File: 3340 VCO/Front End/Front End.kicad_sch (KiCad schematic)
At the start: 32 parts, among them J1 AudioJack2_SwitchT, J2 AudioJack2_SwitchT, J3 AudioJack2_SwitchT, J4 AudioJack2_SwitchT, J5 AudioJack2_SwitchT, J6 Conn_01x19, J7 AudioJack2_SwitchT, J8 AudioJack2_SwitchT, J9 AudioJack2_SwitchT, SW1 SW_SPDT

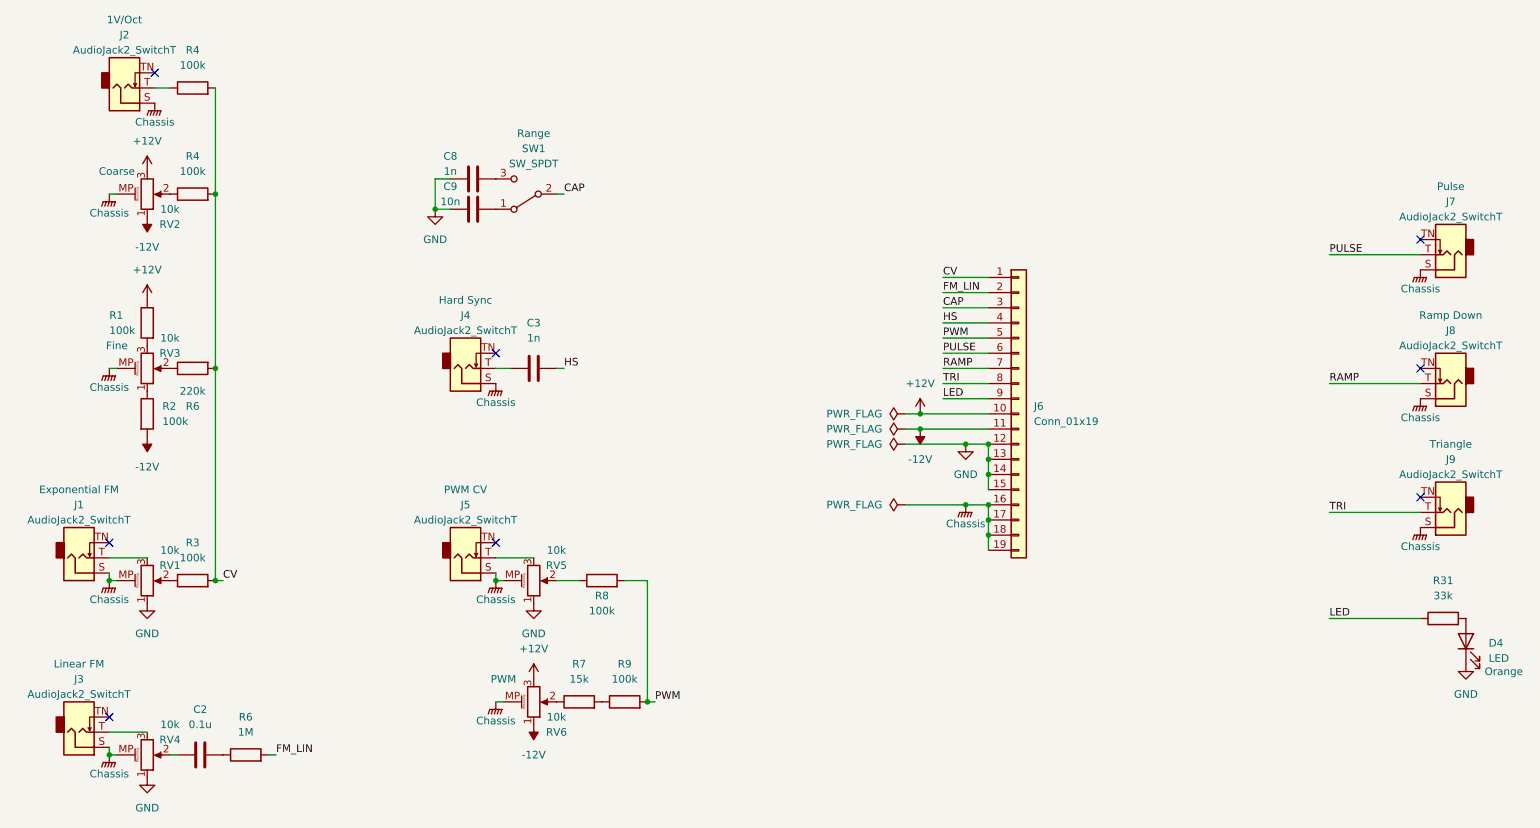
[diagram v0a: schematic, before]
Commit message: Add precision R and C notes, update -5V regulator
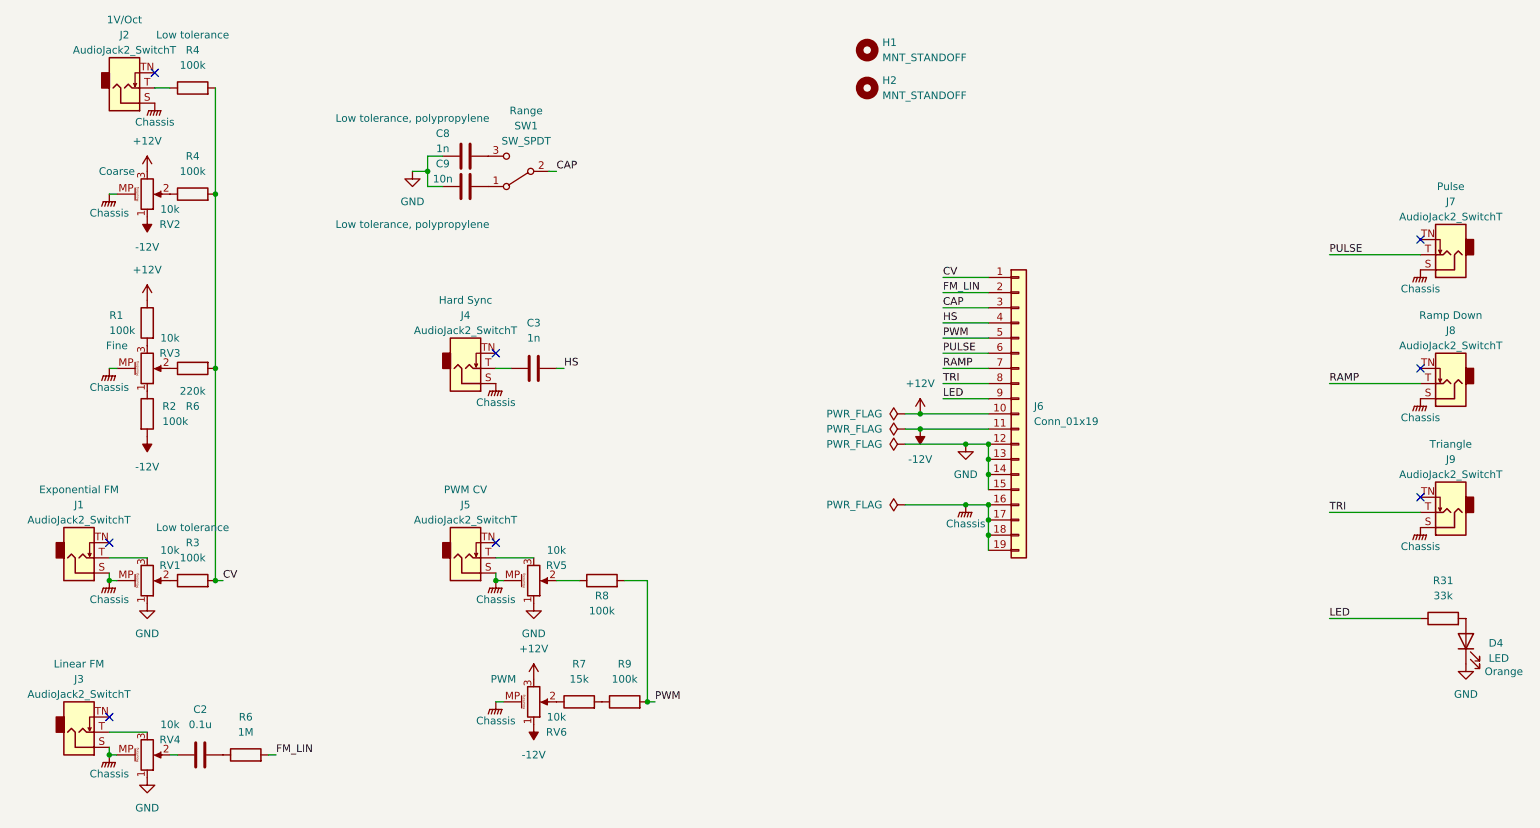
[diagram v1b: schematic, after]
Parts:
- added H1, H2: MNT_STANDOFF, 0_MountingHole:MountingHole_Pitch7.5mm_Drill3.4mm, symbol Mechanical:MountingHole
- C8, C9: Notes (none) -> Low tolerance, polypropylene
- R3, R4: Notes (none) -> Low tolerance
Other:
- moved on the sheet: C8, C9, SW1
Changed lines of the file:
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@@
   (junction (at 34.29 124.46) (diameter 0) (color 0 0 0 0)
   )
+  (junction (at 87.63 55.88) (diameter 0) (color 0 0 0 0)
+  )
   (junction (at 124.46 144.78) (diameter 0) (color 0 0 0 0)
   )
@@
   )
   (junction (at 177.8 101.6) (diameter 0) (color 0 0 0 0)
-  )
-  (junction (at 88.9 62.23) (diameter 0) (color 0 0 0 0)
   )
   (junction (at 181.61 114.3) (diameter 0) (color 0 0 0 0)
@@
     (stroke (width 0) (type default))
   )
-  (wire (pts (xy 88.9 57.15) (xy 88.9 62.23))
+  (wire (pts (xy 87.63 53.34) (xy 87.63 55.88))
     (stroke (width 0) (type default))
   )
@@
     (stroke (width 0) (type default))
   )
+  (wire (pts (xy 87.63 55.88) (xy 87.63 58.42))
+    (stroke (width 0) (type default))
+  )
   (wire (pts (xy 181.61 104.14) (xy 181.61 106.68))
     (stroke (width 0) (type default))
@@
     (stroke (width 0) (type default))
   )
+  (wire (pts (xy 85.09 55.88) (xy 87.63 55.88))
+    (stroke (width 0) (type default))
+  )
   (wire (pts (xy 124.46 144.78) (xy 125.73 144.78))
     (stroke (width 0) (type default))
@@
     (stroke (width 0) (type default))
   )
-  (wire (pts (xy 88.9 57.15) (xy 91.44 57.15))
-    (stroke (width 0) (type default))
-  )
-  (wire (pts (xy 110.49 59.69) (xy 109.22 59.69))
+  (wire (pts (xy 87.63 53.34) (xy 90.17 53.34))
+    (stroke (width 0) (type default))
+  )
+  (wire (pts (xy 109.22 55.88) (xy 107.95 55.88))
     (stroke (width 0) (type default))
   )
@@
     (stroke (width 0) (type default))
   )
-  (wire (pts (xy 88.9 62.23) (xy 91.44 62.23))
+  (wire (pts (xy 87.63 58.42) (xy 90.17 58.42))
     (stroke (width 0) (type default))
   )
@@
     (effects (font (size 1.27 1.27)) (justify left bottom))
   )
-  (label "CAP" (at 110.49 59.69 0) (fields_autoplaced)
+  (label "CAP" (at 109.22 55.88 0) (fields_autoplaced)
     (effects (font (size 1.27 1.27)) (justify left bottom))
   )
@@
     (effects (font (size 1.27 1.27)) (justify left bottom))
   )
-  (symbol (lib_id "Switch:SW_SPDT") (at 104.14 59.69 180) (unit 1)
-    (in_bom yes) (on_board yes) (dnp no)
-    (property "Reference" "SW1" (at 105.41 52.07 0)
-      (effects (font (size 1.27 1.27)))
-    )
-    (property "Value" "SW_SPDT" (at 105.41 54.61 0)
-      (effects (font (size 1.27 1.27)))
-    )
-    (property "Footprint" "0_Switch_THT:MTS-102_MTS-103_MTS-112_MTS-113_MTS-123" (at 104.14 59.69 0)
-      (effects (font (size 1.27 1.27)) hide)
-    )
-    (property "Datasheet" "~" (at 104.14 59.69 0)
-      (effects (font (size 1.27 1.27)) hide)
-    )
-    (property "Notes" "Range" (at 105.41 49.53 0)
+  (symbol (lib_id "Switch:SW_SPDT") (at 102.87 55.88 180) (unit 1)
+    (in_bom yes) (on_board yes) (dnp no)
+    (property "Reference" "SW1" (at 104.14 48.26 0)
+      (effects (font (size 1.27 1.27)))
+    )
+    (property "Value" "SW_SPDT" (at 104.14 50.8 0)
+      (effects (font (size 1.27 1.27)))
+    )
+    (property "Footprint" "0_Switch_THT:MTS-102_MTS-103_MTS-112_MTS-113_MTS-123" (at 102.87 55.88 0)
+      (effects (font (size 1.27 1.27)) hide)
+    )
+    (property "Datasheet" "~" (at 102.87 55.88 0)
+      (effects (font (size 1.27 1.27)) hide)
+    )
+    (property "Notes" "Range" (at 104.14 45.72 0)
       (effects (font (size 1.27 1.27)))
     )
@@
         (path "/a1c7a80e-571d-4d37-b0fe-6f3972cbd9bc"
           (reference "#PWR010") (unit 1)
+        )
+      )
+    )
+  )
+  (symbol (lib_id "Mechanical:MountingHole") (at 161.29 35.56 0) (unit 1)
+    (in_bom yes) (on_board yes) (dnp no) (fields_autoplaced)
+    (property "Reference" "H1" (at 163.83 34.29 0)
+      (effects (font (size 1.27 1.27)) (justify left))
+    )
+    (property "Value" "MNT_STANDOFF" (at 163.83 36.83 0)
+      (effects (font (size 1.27 1.27)) (justify left))
+    )
+    (property "Footprint" "0_MountingHole:MountingHole_Pitch7.5mm_Drill3.4mm" (at 161.29 35.56 0)
+      (effects (font (size 1.27 1.27)) hide)
+    )
+    (property "Datasheet" "~" (at 161.29 35.56 0)
+      (effects (font (size 1.27 1.27)) hide)
+    )
+    (instances
+      (project "Front End"
+        (path "/a1c7a80e-571d-4d37-b0fe-6f3972cbd9bc"
+          (reference "H1") (unit 1)
         )
       )
@@
     )
   )
-  (symbol (lib_id "Device:C") (at 95.25 62.23 90) (unit 1)
-    (in_bom yes) (on_board yes) (dnp no)
-    (property "Reference" "C9" (at 91.44 58.42 90)
-      (effects (font (size 1.27 1.27)))
-    )
-    (property "Value" "10n" (at 91.44 60.96 90)
-      (effects (font (size 1.27 1.27)))
-    )
-    (property "Footprint" "0_Capacitor_THT:C_Disc_D5.5mm_W2.5mm_P2.50mm" (at 99.06 61.2648 0)
-      (effects (font (size 1.27 1.27)) hide)
-    )
-    (property "Datasheet" "~" (at 95.25 62.23 0)
-      (effects (font (size 1.27 1.27)) hide)
+  (symbol (lib_id "Device:C") (at 93.98 58.42 90) (unit 1)
+    (in_bom yes) (on_board yes) (dnp no)
+    (property "Reference" "C9" (at 90.17 54.61 90)
+      (effects (font (size 1.27 1.27)))
+    )
+    (property "Value" "10n" (at 90.17 57.15 90)
+      (effects (font (size 1.27 1.27)))
+    )
+    (property "Footprint" "0_Capacitor_THT:C_Disc_D5.5mm_W2.5mm_P2.50mm" (at 97.79 57.4548 0)
+      (effects (font (size 1.27 1.27)) hide)
+    )
+    (property "Datasheet" "~" (at 93.98 58.42 0)
+      (effects (font (size 1.27 1.27)) hide)
+    )
+    (property "Notes" "Low tolerance, polypropylene" (at 85.09 64.77 90)
+      (effects (font (size 1.27 1.27)))
     )
     (pin "1")
@@
         (path "/a1c7a80e-571d-4d37-b0fe-6f3972cbd9bc"
           (reference "#FLG04") (unit 1)
+        )
+      )
+    )
+  )
+  (symbol (lib_id "Mechanical:MountingHole") (at 161.29 41.91 0) (unit 1)
+    (in_bom yes) (on_board yes) (dnp no) (fields_autoplaced)
+    (property "Reference" "H2" (at 163.83 40.64 0)
+      (effects (font (size 1.27 1.27)) (justify left))
+    )
+    (property "Value" "MNT_STANDOFF" (at 163.83 43.18 0)
+      (effects (font (size 1.27 1.27)) (justify left))
+    )
+    (property "Footprint" "0_MountingHole:MountingHole_Pitch7.5mm_Drill3.4mm" (at 161.29 41.91 0)
+      (effects (font (size 1.27 1.27)) hide)
+    )
+    (property "Datasheet" "~" (at 161.29 41.91 0)
+      (effects (font (size 1.27 1.27)) hide)
+    )
+    (instances
+      (project "Front End"
+        (path "/a1c7a80e-571d-4d37-b0fe-6f3972cbd9bc"
+          (reference "H2") (unit 1)
         )
       )
@@
       (effects (font (size 1.27 1.27)) hide)
     )
+    (property "Notes" "Low tolerance" (at 48.26 33.02 90)
+      (effects (font (size 1.27 1.27)))
+    )
     (pin "1")
     (pin "2")
@@
     )
   )
-  (symbol (lib_id "Device:C") (at 95.25 57.15 90) (unit 1)
-    (in_bom yes) (on_board yes) (dnp no)
-    (property "Reference" "C8" (at 91.44 53.34 90)
-      (effects (font (size 1.27 1.27)))
-    )
-    (property "Value" "1n" (at 91.44 55.88 90)
-      (effects (font (size 1.27 1.27)))
-    )
-    (property "Footprint" "0_Capacitor_THT:C_Disc_D5.5mm_W2.5mm_P2.50mm" (at 99.06 56.1848 0)
-      (effects (font (size 1.27 1.27)) hide)
-    )
-    (property "Datasheet" "~" (at 95.25 57.15 0)
-      (effects (font (size 1.27 1.27)) hide)
+  (symbol (lib_id "Device:C") (at 93.98 53.34 90) (unit 1)
+    (in_bom yes) (on_board yes) (dnp no)
+    (property "Reference" "C8" (at 90.17 49.53 90)
+      (effects (font (size 1.27 1.27)))
+    )
+    (property "Value" "1n" (at 90.17 52.07 90)
+      (effects (font (size 1.27 1.27)))
+    )
+    (property "Footprint" "0_Capacitor_THT:C_Disc_D5.5mm_W2.5mm_P2.50mm" (at 97.79 52.3748 0)
+      (effects (font (size 1.27 1.27)) hide)
+    )
+    (property "Datasheet" "~" (at 93.98 53.34 0)
+      (effects (font (size 1.27 1.27)) hide)
+    )
+    (property "Notes" "Low tolerance, polypropylene" (at 85.09 46.99 90)
+      (effects (font (size 1.27 1.27)))
     )
     (pin "1")
@@
     )
   )
-  (symbol (lib_id "power:GND") (at 88.9 62.23 0) (unit 1)
-    (in_bom yes) (on_board yes) (dnp no) (fields_autoplaced)
-    (property "Reference" "#PWR020" (at 88.9 68.58 0)
-      (effects (font (size 1.27 1.27)) hide)
-    )
-    (property "Value" "GND" (at 88.9 67.31 0)
-      (effects (font (size 1.27 1.27)))
-    )
-    (property "Footprint" "" (at 88.9 62.23 0)
-      (effects (font (size 1.27 1.27)) hide)
-    )
-    (property "Datasheet" "" (at 88.9 62.23 0)
+  (symbol (lib_id "power:GND") (at 85.09 55.88 0) (unit 1)
+    (in_bom yes) (on_board yes) (dnp no) (fields_autoplaced)
+    (property "Reference" "#PWR020" (at 85.09 62.23 0)
+      (effects (font (size 1.27 1.27)) hide)
+    )
+    (property "Value" "GND" (at 85.09 60.96 0)
+      (effects (font (size 1.27 1.27)))
+    )
+    (property "Footprint" "" (at 85.09 55.88 0)
+      (effects (font (size 1.27 1.27)) hide)
+    )
+    (property "Datasheet" "" (at 85.09 55.88 0)
       (effects (font (size 1.27 1.27)) hide)
     )
@@
       (effects (font (size 1.27 1.27)) hide)
     )
-    (pin "1")
+    (property "Notes" "Low tolerance" (at 48.26 115.57 90)
+      (effects (font (size 1.27 1.27)))
+    )
+    (pin "1")

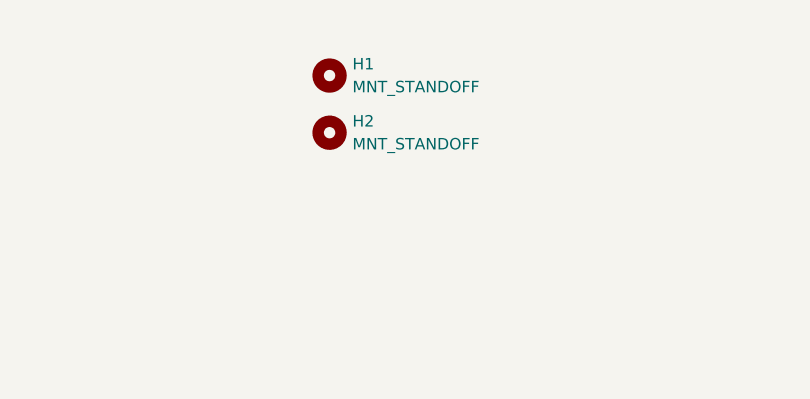
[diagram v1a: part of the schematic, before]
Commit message: Update VCO capacitor selection
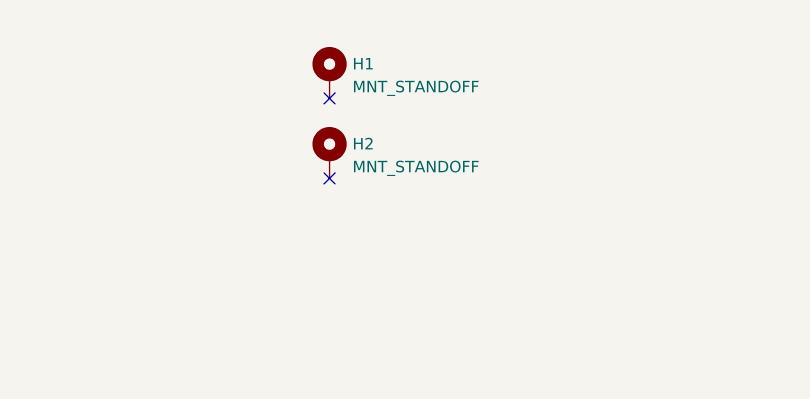
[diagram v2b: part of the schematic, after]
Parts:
- C8: footprint 0_Capacitor_THT:C_Disc_D5.5mm_W2.5mm_P2.50mm -> 0_Capacitor_THT:C_Rect_L7.2mm_W4.5mm_P5.00mm
- C9: footprint 0_Capacitor_THT:C_Disc_D5.5mm_W2.5mm_P2.50mm -> 0_Capacitor_THT:C_Rect_L7.5mm_W5.5mm_P5.00mm
- H1, H2: symbol Mechanical:MountingHole -> Mechanical:MountingHole_Pad
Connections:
- no-connect marks 8 -> 10
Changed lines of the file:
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@@
   (no_connect (at 41.91 39.37))
   (no_connect (at 99.06 118.11))
+  (no_connect (at 161.29 38.1))
+  (no_connect (at 161.29 46.99))
   (no_connect (at 34.29 147.32))
   (no_connect (at 34.29 118.11))
@@
     )
   )
-  (symbol (lib_id "Mechanical:MountingHole") (at 161.29 35.56 0) (unit 1)
+  (symbol (lib_id "Mechanical:MountingHole_Pad") (at 161.29 35.56 0) (unit 1)
     (in_bom yes) (on_board yes) (dnp no) (fields_autoplaced)
     (property "Reference" "H1" (at 163.83 34.29 0)
@@
       (effects (font (size 1.27 1.27)) hide)
     )
+    (pin "1")
     (instances
       (project "Front End"
@@
       (effects (font (size 1.27 1.27)))
     )
-    (property "Footprint" "0_Capacitor_THT:C_Disc_D5.5mm_W2.5mm_P2.50mm" (at 97.79 57.4548 0)
+    (property "Footprint" "0_Capacitor_THT:C_Rect_L7.5mm_W5.5mm_P5.00mm" (at 97.79 57.4548 0)
       (effects (font (size 1.27 1.27)) hide)
     )
@@
     )
   )
-  (symbol (lib_id "Mechanical:MountingHole") (at 161.29 41.91 0) (unit 1)
-    (in_bom yes) (on_board yes) (dnp no) (fields_autoplaced)
-    (property "Reference" "H2" (at 163.83 40.64 0)
+  (symbol (lib_id "Mechanical:MountingHole_Pad") (at 161.29 44.45 0) (unit 1)
+    (in_bom yes) (on_board yes) (dnp no) (fields_autoplaced)
+    (property "Reference" "H2" (at 163.83 43.18 0)
       (effects (font (size 1.27 1.27)) (justify left))
     )
-    (property "Value" "MNT_STANDOFF" (at 163.83 43.18 0)
+    (property "Value" "MNT_STANDOFF" (at 163.83 45.72 0)
       (effects (font (size 1.27 1.27)) (justify left))
     )
-    (property "Footprint" "0_MountingHole:MountingHole_Pitch7.5mm_Drill3.4mm" (at 161.29 41.91 0)
-      (effects (font (size 1.27 1.27)) hide)
-    )
-    (property "Datasheet" "~" (at 161.29 41.91 0)
-      (effects (font (size 1.27 1.27)) hide)
-    )
+    (property "Footprint" "0_MountingHole:MountingHole_Pitch7.5mm_Drill3.4mm" (at 161.29 44.45 0)
+      (effects (font (size 1.27 1.27)) hide)
+    )
+    (property "Datasheet" "~" (at 161.29 44.45 0)
+      (effects (font (size 1.27 1.27)) hide)
+    )
+    (pin "1")
     (instances
       (project "Front End"
@@
       (effects (font (size 1.27 1.27)))
     )
-    (property "Footprint" "0_Capacitor_THT:C_Disc_D5.5mm_W2.5mm_P2.50mm" (at 97.79 52.3748 0)
-      (effects (font (size 1.27 1.27)) hide)
-    )
+    (property "Footprint" "0_Capacitor_THT:C_Rect_L7.2mm_W4.5mm_P5.00mm" (at 97.79 52.3748 0)
+      (effects (font (size 1.27 1.27)) hide)
+    )
